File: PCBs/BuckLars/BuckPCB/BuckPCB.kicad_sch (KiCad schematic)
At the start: 78 parts, among them J1 POWER_IN, J2 Program_header, J3 5V, J4 12V, J7 Conn_01x08_Pin, Q1 IRLIZ44N, Q2 IRLIZ44N, Q3 IRLIZ44N, Q4 IRLIZ44N, SW1 RESET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

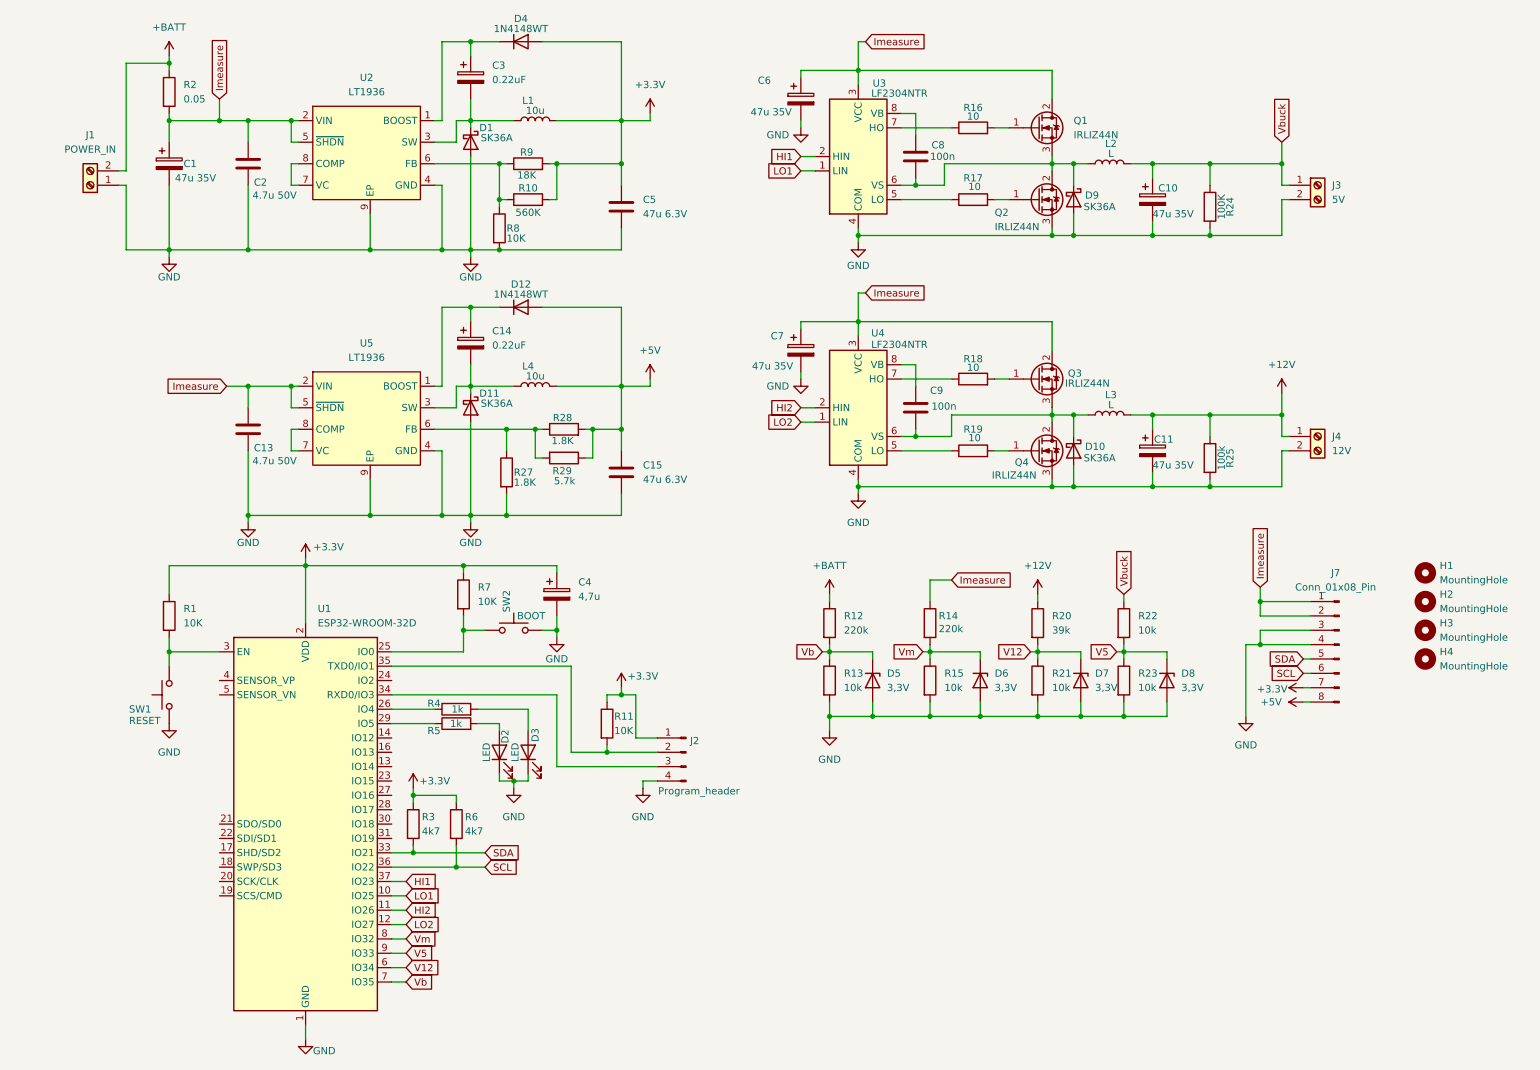
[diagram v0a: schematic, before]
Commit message: added qr code and status leds
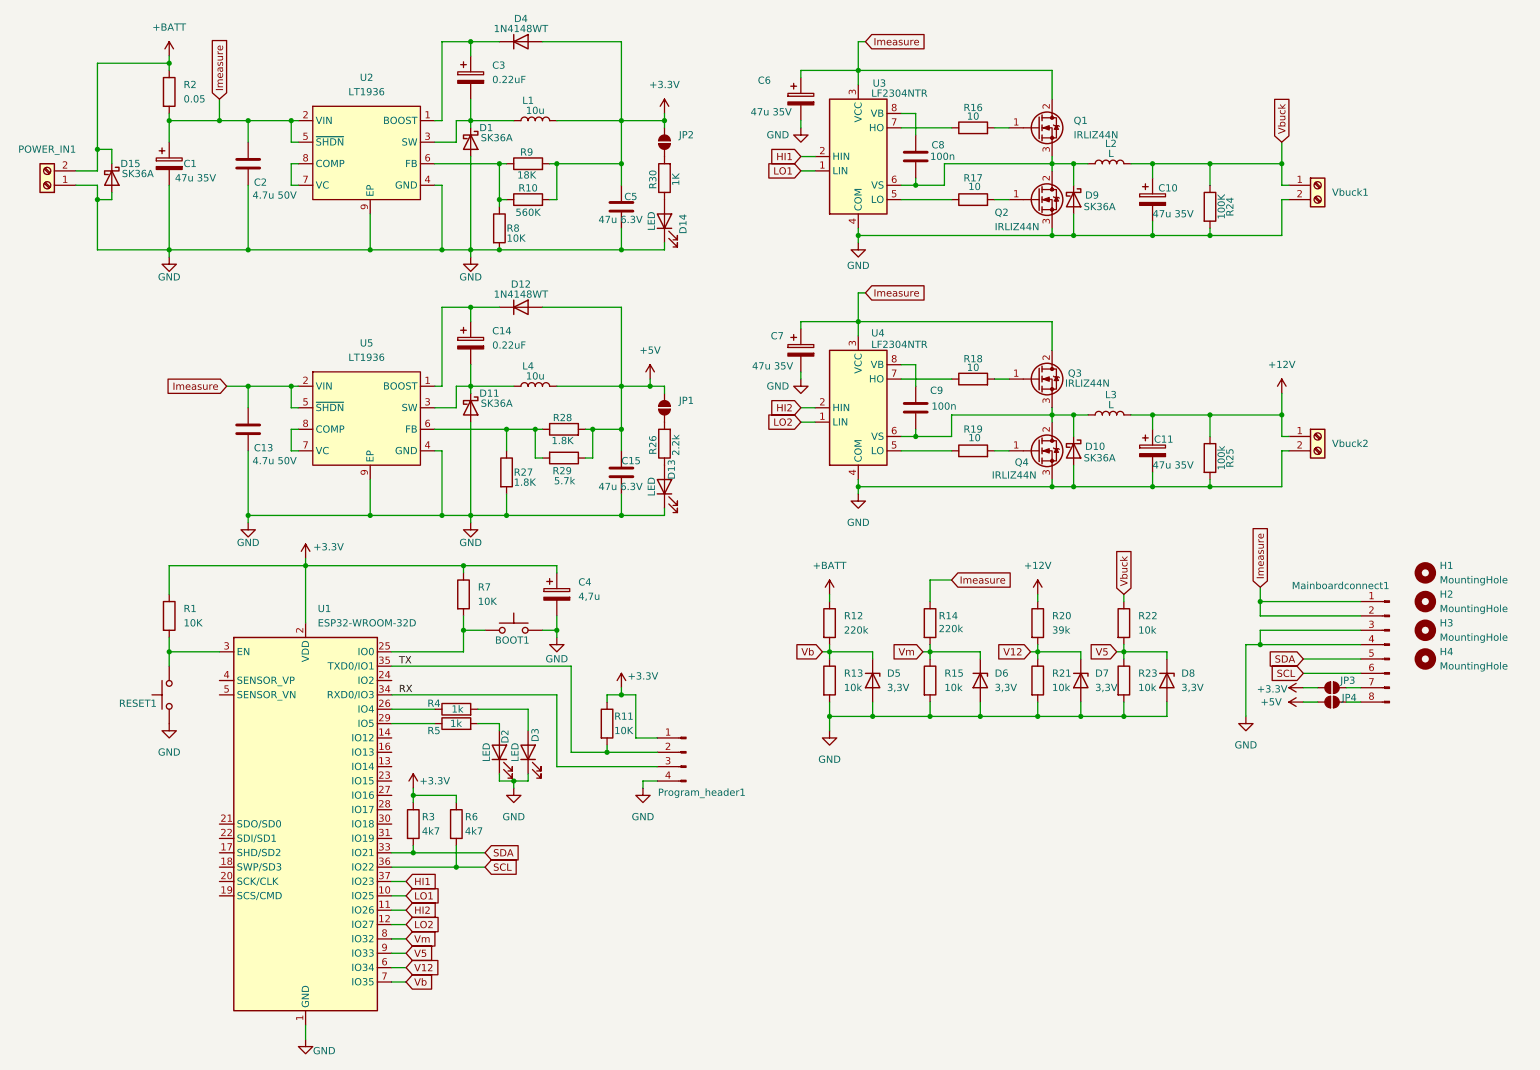
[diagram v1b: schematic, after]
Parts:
- added D13, D14: LED, LED_SMD:LED_0805_2012Metric, symbol Device:LED
- added D15: SK36A, Diode_SMD:D_SMC-RM10_Universal_Handsoldering, symbol Device:D_Schottky
- added JP1, JP2, JP3, JP4: SolderJumper_2_Open, Jumper:SolderJumper-2_P1.3mm_Open_TrianglePad1.0x1.5mm, symbol Jumper:SolderJumper_2_Open
- added R26: 2.2k, Resistor_SMD:R_1206_3216Metric_Pad1.30x1.75mm_HandSolder, symbol Device:R
- added R30: 1K, Resistor_SMD:R_1206_3216Metric_Pad1.30x1.75mm_HandSolder, symbol Device:R
- Vbuck1: renamed from J3; value 5V -> Vbuck
- renumbered SW2 to BOOT1, J7 to Mainboardconnect1, J1 to POWER_IN1, J2 to Program_header1, SW1 to RESET1, J4 to Vbuck2
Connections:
- net +3.3V: now also JP2.2 (B), JP3.2 (B); no longer Mainboardconnect1.7 (Pin_7)
- net +5V: now also JP1.2 (B), JP4.2 (B); no longer Mainboardconnect1.8 (Pin_8)
- net +BATT: now also D15.1 (K)
- net GND: now also D13.1 (K), D14.1 (K), D15.2 (A)
- net RX: now reaches Program_header1.3 (Pin_3), U1.34 (RXD0/IO3)
- net TX: now reaches Program_header1.2 (Pin_2), R11.2, U1.35 (TXD0/IO1)
- new net: D13.2 (A), R26.1
- new net: JP1.1 (A), R26.2
- new net: JP3.1 (A), Mainboardconnect1.7 (Pin_7)
- new net: JP4.1 (A), Mainboardconnect1.8 (Pin_8)
- new net: D14.2 (A), R30.1
- new net: JP2.1 (A), R30.2
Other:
- moved on the sheet: Mainboardconnect1, POWER_IN1

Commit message: generated gerbers
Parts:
- added JP5: SolderJumper_2_Open, Jumper:SolderJumper-2_P1.3mm_Open_TrianglePad1.0x1.5mm, symbol Jumper:SolderJumper_2_Open
- added POWER_IN2: POWER_IN, TerminalBlock:TerminalBlock_MaiXu_MX126-5.0-02P_1x02_P5.00mm, symbol Connector:Screw_Terminal_01x02
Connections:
- net +BATT: now also JP5.2 (B), POWER_IN2.2 (Pin_2)
- net GND: now also POWER_IN2.1 (Pin_1)
- net Imeasure: now also JP5.1 (A)
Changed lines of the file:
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@@
 	)
 	(junction
+		(at 29.21 31.75)
+		(diameter 0)
+		(color 0 0 0 0)
+	)
+	(junction
 		(at 226.06 52.07)
 		(diameter 0)
@@
 	)
 	(junction
+		(at 26.67 40.64)
+		(diameter 0)
+		(color 0 0 0 0)
+	)
+	(junction
 		(at 234.95 124.46)
 		(diameter 0)
@@
 	)
 	(junction
+		(at 29.21 52.07)
+		(diameter 0)
+		(color 0 0 0 0)
+	)
+	(junction
 		(at 121.92 86.36)
 		(diameter 0)
@@
 	(wire
 		(pts
+			(xy 25.4 49.53) (xy 26.67 49.53)
+		)
+		(stroke
+			(width 0)
+			(type default)
+		)
+	)
+	(wire
+		(pts
 			(xy 109.22 39.37) (xy 110.49 39.37)
 		)
@@
 	(wire
 		(pts
+			(xy 29.21 31.75) (xy 33.02 31.75)
+		)
+		(stroke
+			(width 0)
+			(type default)
+		)
+	)
+	(wire
+		(pts
 			(xy 226.06 50.8) (xy 226.06 52.07)
 		)
@@
 	(wire
 		(pts
+			(xy 25.4 52.07) (xy 29.21 52.07)
+		)
+		(stroke
+			(width 0)
+			(type default)
+		)
+	)
+	(wire
+		(pts
 			(xy 81.28 184.15) (xy 83.82 184.15)
 		)
@@
 	(wire
 		(pts
-			(xy 29.21 45.72) (xy 29.21 54.61)
+			(xy 29.21 45.72) (xy 29.21 52.07)
 		)
 		(stroke
@@
 	(wire
 		(pts
+			(xy 29.21 31.75) (xy 29.21 36.83)
+		)
+		(stroke
+			(width 0)
+			(type default)
+		)
+	)
+	(wire
+		(pts
 			(xy 55.88 78.74) (xy 63.5 78.74)
 		)
@@
 	(wire
 		(pts
+			(xy 29.21 52.07) (xy 29.21 54.61)
+		)
+		(stroke
+			(width 0)
+			(type default)
+		)
+	)
+	(wire
+		(pts
 			(xy 81.28 173.99) (xy 83.82 173.99)
 		)
@@
 	(wire
 		(pts
-			(xy 29.21 21.59) (xy 29.21 36.83)
+			(xy 29.21 21.59) (xy 29.21 31.75)
+		)
+		(stroke
+			(width 0)
+			(type default)
+		)
+	)
+	(wire
+		(pts
+			(xy 26.67 49.53) (xy 26.67 40.64)
 		)
 		(stroke
@@
 	(wire
 		(pts
-			(xy 25.4 40.64) (xy 29.21 40.64)
+			(xy 25.4 40.64) (xy 26.67 40.64)
 		)
 		(stroke
@@
 	(wire
 		(pts
+			(xy 26.67 40.64) (xy 29.21 40.64)
+		)
+		(stroke
+			(width 0)
+			(type default)
+		)
+	)
+	(wire
+		(pts
 			(xy 238.76 90.17) (xy 238.76 96.52)
 		)
@@
 	(wire
 		(pts
+			(xy 38.1 31.75) (xy 41.91 31.75)
+		)
+		(stroke
+			(width 0)
+			(type default)
+		)
+	)
+	(wire
+		(pts
 			(xy 127 78.74) (xy 121.92 78.74)
 		)
@@
 	)
 	(symbol
+		(lib_name "SolderJumper_2_Open_1")
+		(lib_id "Jumper:SolderJumper_2_Open")
+		(at 35.56 31.75 180)
+		(unit 1)
+		(exclude_from_sim no)
+		(in_bom no)
+		(on_board yes)
+		(dnp no)
+		(property "Reference" "JP5"
+			(at 38.354 30.48 0)
+			(effects
+				(font
+					(size 1.27 1.27)
+				)
+			)
+		)
+		(property "Value" "SolderJumper_2_Open"
+			(at 36.8299 29.21 90)
+			(effects
+				(font
+					(size 1.27 1.27)
+				)
+				(justify right)
+				(hide yes)
+			)
+		)
+		(property "Footprint" "Jumper:SolderJumper-2_P1.3mm_Open_TrianglePad1.0x1.5mm"
+			(at 35.56 31.75 0)
+			(effects
+				(font
+					(size 1.27 1.27)
+				)
+				(hide yes)
+			)
+		)
+		(property "Datasheet" "~"
+			(at 35.56 31.75 0)
+			(effects
+				(font
+					(size 1.27 1.27)
+				)
+				(hide yes)
+			)
+		)
+		(property "Description" "Solder Jumper, 2-pole, open"
+			(at 35.56 31.75 0)
+			(effects
+				(font
+					(size 1.27 1.27)
+				)
+				(hide yes)
+			)
+		)
+		(pin "1"
+		)
+		(pin "2"
+		)
+		(instances
+			(project "BuckPCB"
+				(path "/091e8063-b3c9-455e-bf2d-57e0600ed10e"
+					(reference "JP5")
+					(unit 1)
+				)
+			)
+		)
+	)
+	(symbol
 		(lib_id "power:+3.3V")
 		(at 85.09 149.86 0)
@@
 					(unit 1)
 				)
+			)
+		)
+	)
+	(symbol
+		(lib_id "Connector:Screw_Terminal_01x02")
+		(at 20.32 52.07 180)
+		(unit 1)
+		(exclude_from_sim no)
+		(in_bom yes)
+		(on_board yes)
+		(dnp no)
+		(fields_autoplaced yes)
+		(property "Reference" "POWER_IN2"
+			(at 20.32 45.72 0)
+			(effects
+				(font
+					(size 1.27 1.27)
+				)
+			)
+		)
+		(property "Value" "POWER_IN"
+			(at 20.32 45.72 0)
+			(effects
+				(font
+					(size 1.27 1.27)
+				)
+				(hide yes)
+			)
+		)
+		(property "Footprint" "TerminalBlock:TerminalBlock_MaiXu_MX126-5.0-02P_1x02_P5.00mm"
+			(at 20.32 52.07 0)
+			(effects
+				(font
+					(size 1.27 1.27)
+				)
+				(hide yes)
+			)
+		)
+		(property "Datasheet" "~"
+			(at 20.32 52.07 0)
+			(effects
+				(font
+					(size 1.27 1.27)
+				)
+				(hide yes)
+			)
+		)
+		(property "Description" "Generic screw terminal, single row, 01x02, script generated (kicad-library-utils/schlib/autogen/connector/)"
+			(at 20.32 52.07 0)
+			(effects
+				(font
+					(size 1.27 1.27)
+				)
+				(hide yes)
+			)
+		)
+		(pin "1"
+		)
+		(pin "2"
+		)
+		(instances
+			(project "BuckPCB"
+				(path "/091e8063-b3c9-455e-bf2d-57e0600ed10e"
+					(reference "POWER_IN2")
+					(unit 1)
+				)

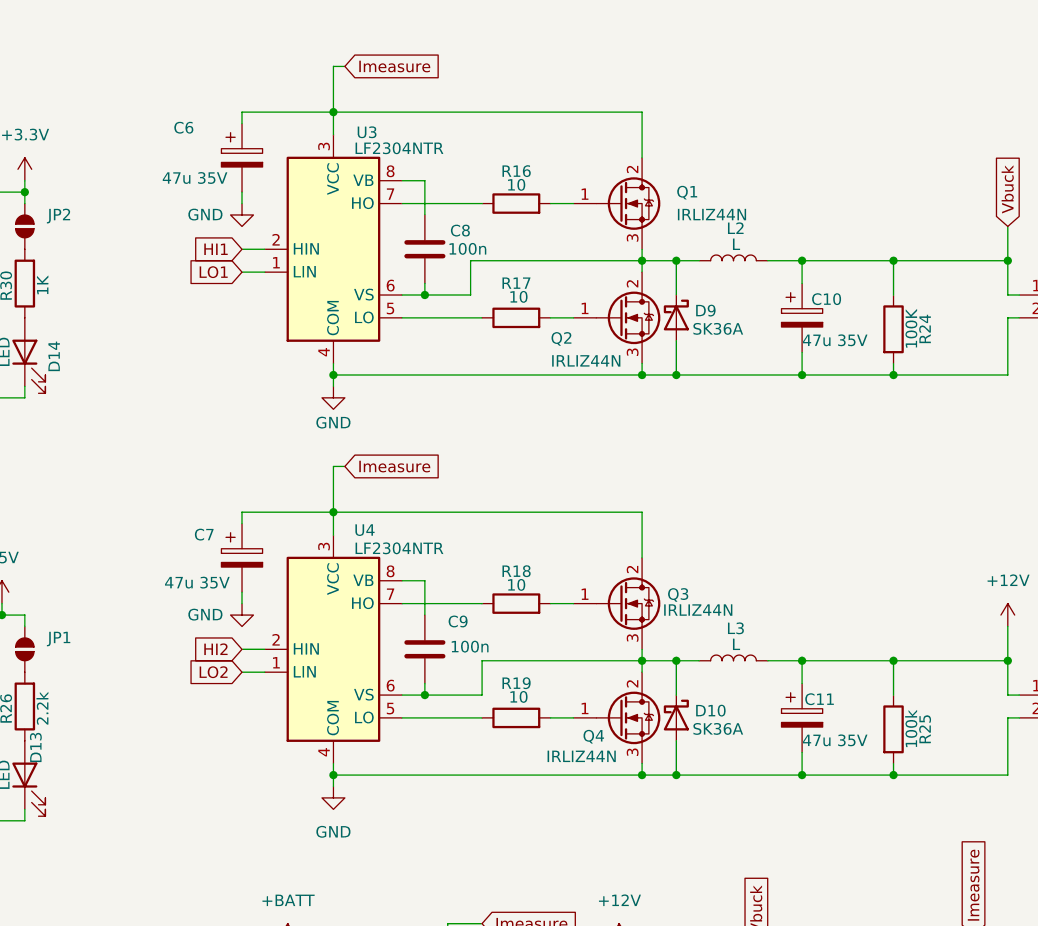
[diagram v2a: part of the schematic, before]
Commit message: changed buck driver circuit
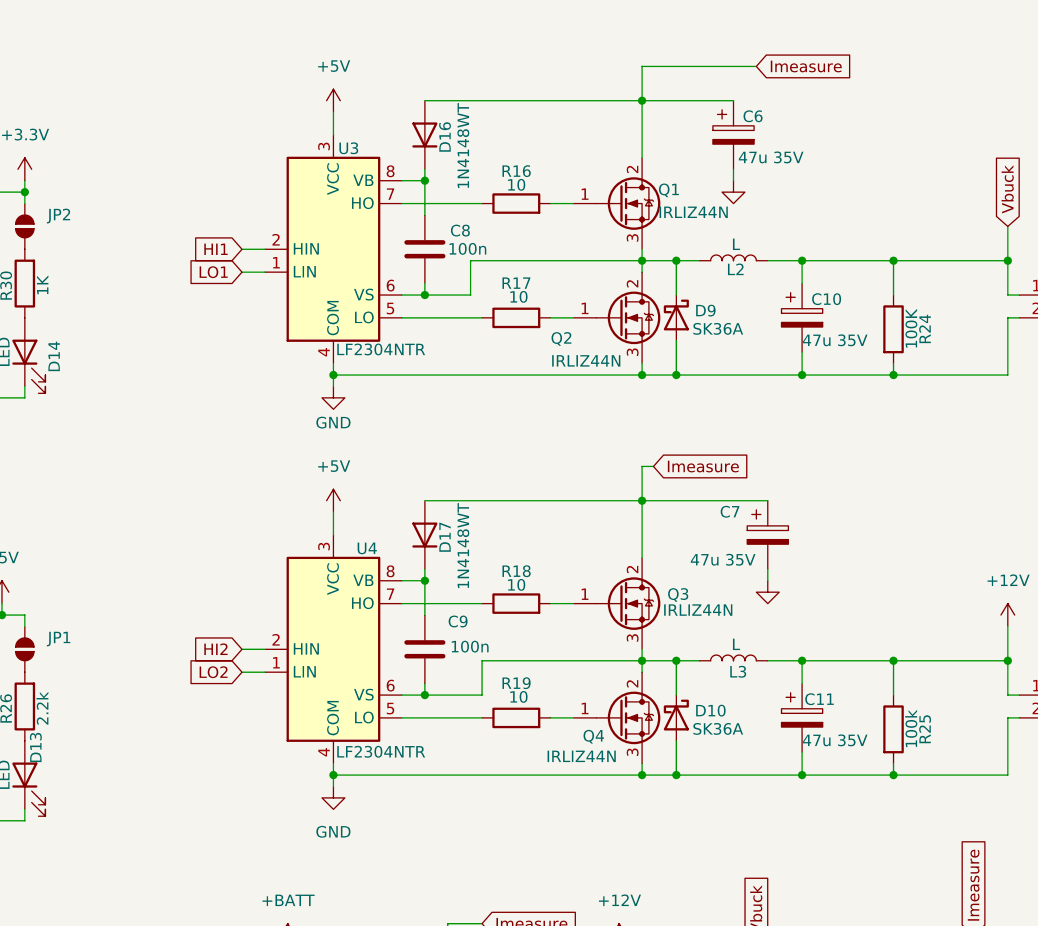
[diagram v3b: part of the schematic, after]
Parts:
- added D16, D17: 1N4148WT, Diode_SMD:D_SOD-523, symbol Diode:1N4148WT
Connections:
- net +5V: now also U3.3 (VCC), U4.3 (VCC)
- net Imeasure: now also D16.2 (A), D17.2 (A); no longer U3.3 (VCC), U4.3 (VCC)
- net at C9.1, U4.8 (VB): now also D17.1 (K)
- net at C8.1, U3.8 (VB): now also D16.1 (K)
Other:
- moved on the sheet: C6, C7
